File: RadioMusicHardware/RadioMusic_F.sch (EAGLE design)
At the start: 30 parts, among them X1 VERT_SD_CARD

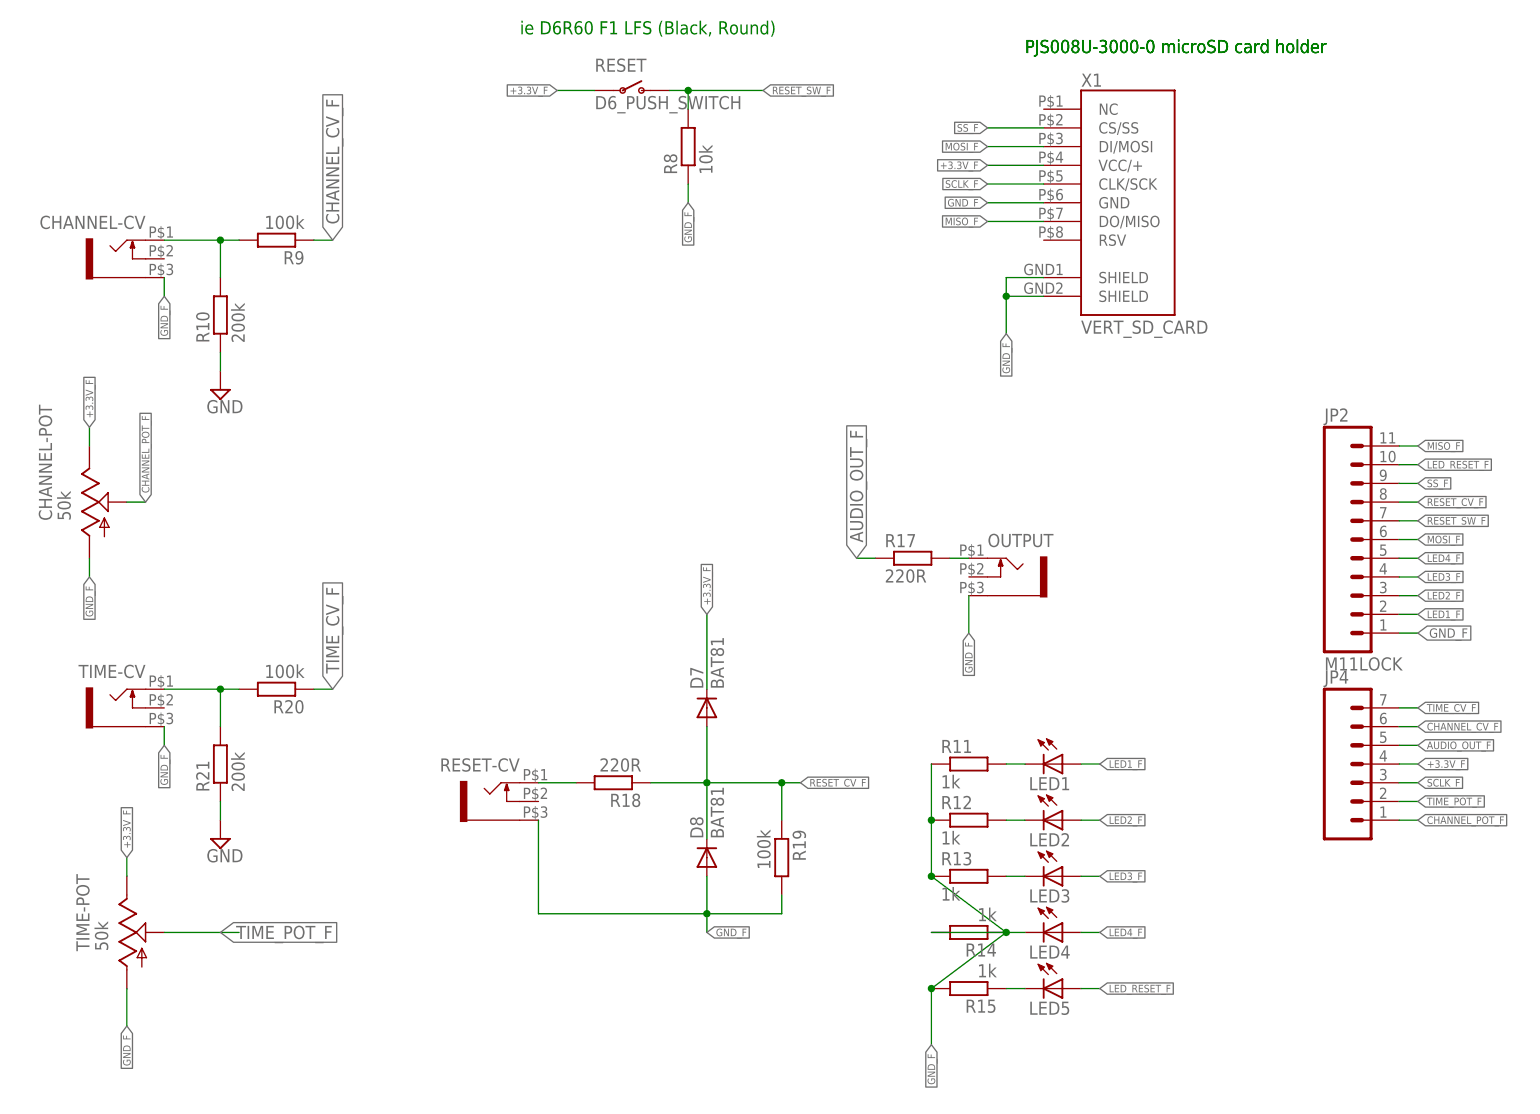
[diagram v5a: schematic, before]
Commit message: Fixed issues on Rev1 proto boards
Diodes changed to BAT42
LED resistors changed to 2k
Ground error on Front board fixed
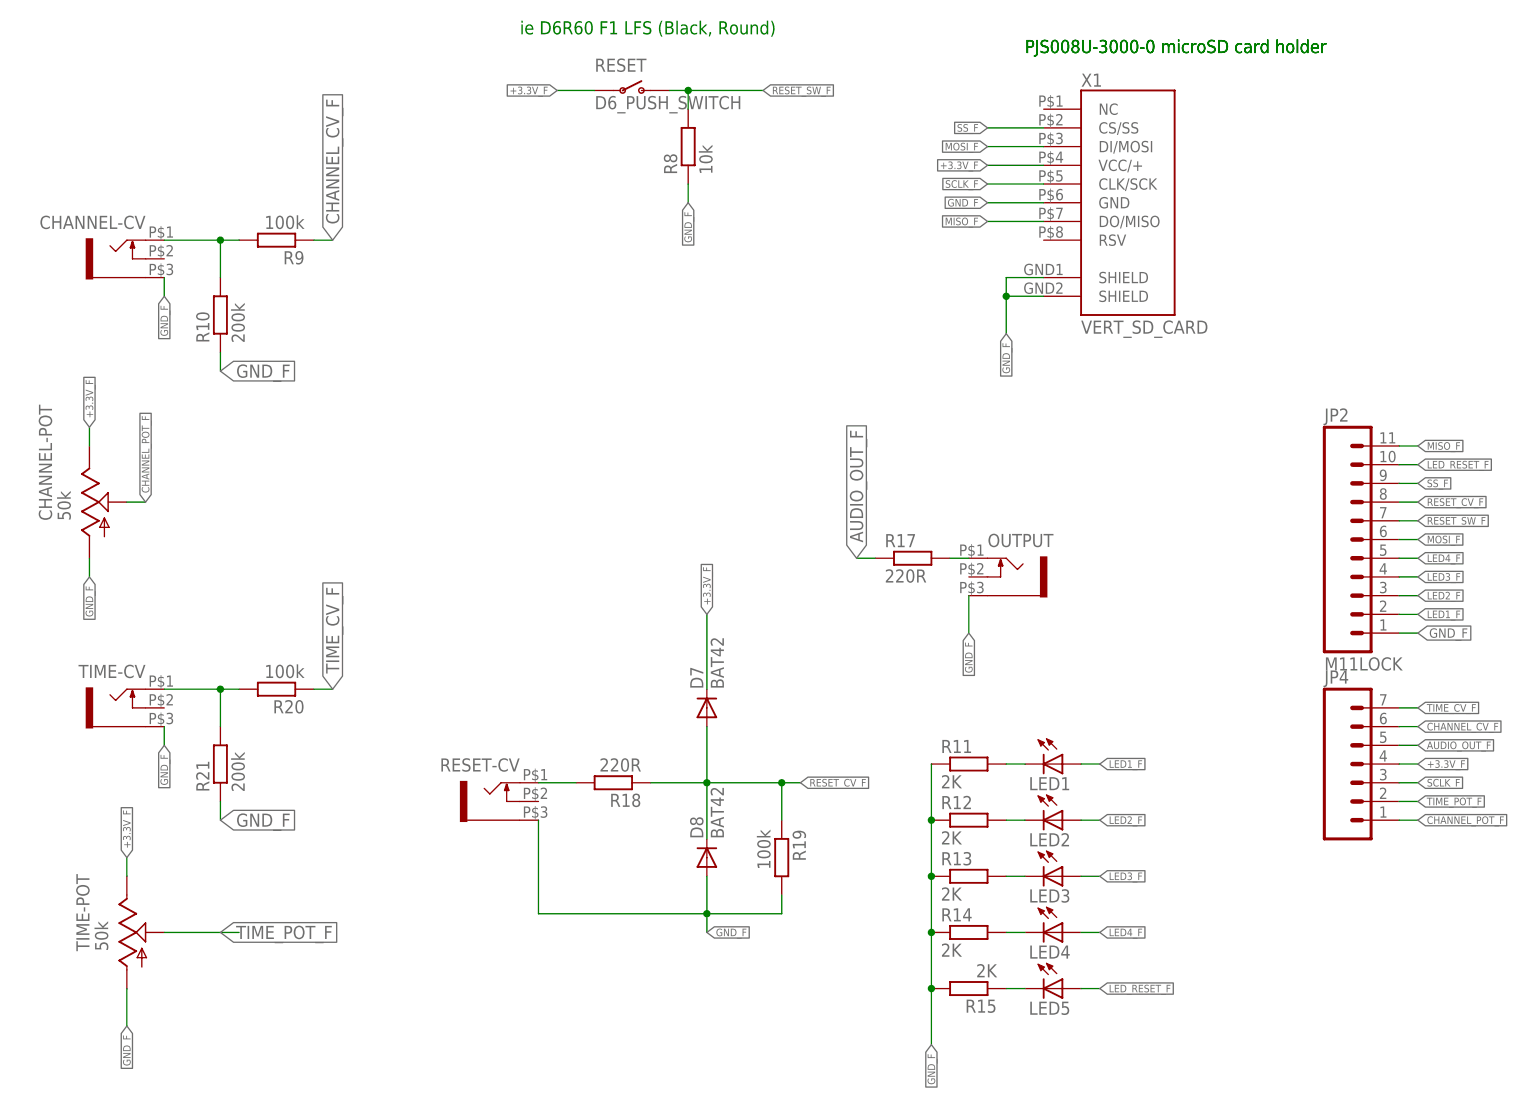
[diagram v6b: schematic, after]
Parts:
- D7, D8: value BAT81 -> BAT42
- R11, R12, R13, R14, R15: value 1k -> 2K
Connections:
- removed net GND: R10.1, R21.1
- net GND_F: now also R10.1, R21.1
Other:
- moved on the sheet: R14
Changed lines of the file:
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@@
 <part name="R9" library="TomW" deviceset="R-EU_" device="STANDARD_RESISTOR" value="100k"/>
 <part name="R10" library="TomW" deviceset="R-EU_" device="STANDARD_RESISTOR" value="200k"/>
-<part name="SUPPLY4" library="supply2" deviceset="GND" device=""/>
 <part name="R17" library="TomW" deviceset="R-EU_" device="STANDARD_RESISTOR" value="220R"/>
 <part name="TIME-POT" library="TomW" deviceset="ALPHA-9MM" device="A" technology="F2" value="50k"/>
@@
 <part name="R20" library="TomW" deviceset="R-EU_" device="STANDARD_RESISTOR" value="100k"/>
 <part name="R21" library="TomW" deviceset="R-EU_" device="STANDARD_RESISTOR" value="200k"/>
-<part name="SUPPLY5" library="supply2" deviceset="GND" device=""/>
-<part name="D7" library="diode" deviceset="BAT81" device=""/>
-<part name="D8" library="diode" deviceset="BAT81" device=""/>
+<part name="D7" library="diode" deviceset="BAT81" device="" value="BAT42"/>
+<part name="D8" library="diode" deviceset="BAT81" device="" value="BAT42"/>
 <part name="R19" library="TomW" deviceset="R-EU_" device="STANDARD_RESISTOR" value="100k"/>
 <part name="R18" library="TomW" deviceset="R-EU_" device="STANDARD_RESISTOR" value="220R"/>
@@
 <part name="LED3" library="TomW" deviceset="LED" device="3MM"/>
 <part name="LED4" library="TomW" deviceset="LED" device="3MM"/>
-<part name="R11" library="TomW" deviceset="R-EU_" device="STANDARD_RESISTOR" value="1k"/>
-<part name="R12" library="TomW" deviceset="R-EU_" device="STANDARD_RESISTOR" value="1k"/>
-<part name="R13" library="TomW" deviceset="R-EU_" device="STANDARD_RESISTOR" value="1k"/>
-<part name="R14" library="TomW" deviceset="R-EU_" device="STANDARD_RESISTOR" value="1k"/>
+<part name="R11" library="TomW" deviceset="R-EU_" device="STANDARD_RESISTOR" value="2K"/>
+<part name="R12" library="TomW" deviceset="R-EU_" device="STANDARD_RESISTOR" value="2K"/>
+<part name="R13" library="TomW" deviceset="R-EU_" device="STANDARD_RESISTOR" value="2K"/>
+<part name="R14" library="TomW" deviceset="R-EU_" device="STANDARD_RESISTOR" value="2K"/>
 <part name="X1" library="TomW" deviceset="VERT_SD_CARD" device=""/>
 <part name="LED5" library="TomW" deviceset="LED" device="3MM"/>
-<part name="R15" library="TomW" deviceset="R-EU_" device="STANDARD_RESISTOR" value="1k"/>
+<part name="R15" library="TomW" deviceset="R-EU_" device="STANDARD_RESISTOR" value="2K"/>
 <part name="JP2" library="SparkFun-Connectors" deviceset="M11" device="LOCK"/>
 <part name="JP4" library="SparkFun-Connectors" deviceset="M07" device="LOCK"/>
@@
 <instance part="R9" gate="G$1" x="50.8" y="116.84" rot="R180"/>
 <instance part="R10" gate="G$1" x="43.18" y="106.68" rot="R90"/>
-<instance part="SUPPLY4" gate="GND" x="43.18" y="96.52"/>
 <instance part="R17" gate="G$1" x="137.16" y="73.66"/>
 <instance part="TIME-POT" gate="G$1" x="30.48" y="22.86"/>
@@
 <instance part="R20" gate="G$1" x="50.8" y="55.88" rot="R180"/>
 <instance part="R21" gate="G$1" x="43.18" y="45.72" rot="R90"/>
-<instance part="SUPPLY5" gate="GND" x="43.18" y="35.56"/>
 <instance part="D7" gate="1" x="109.22" y="53.34" rot="R90"/>
 <instance part="D8" gate="1" x="109.22" y="33.02" rot="R90"/>
@@
 <instance part="R12" gate="G$1" x="144.78" y="38.1"/>
 <instance part="R13" gate="G$1" x="144.78" y="30.48"/>
-<instance part="R14" gate="G$1" x="144.78" y="22.86" rot="R180"/>
+<instance part="R14" gate="G$1" x="144.78" y="22.86"/>
 <instance part="X1" gate="G$1" x="162.56" y="121.92"/>
 <instance part="LED5" gate="G$1" x="157.48" y="15.24" rot="R270"/>
@@
 </busses>
 <nets>
-<net name="GND" class="2">
-<segment>
-<pinref part="R10" gate="G$1" pin="1"/>
-<wire x1="43.18" y1="101.6" x2="43.18" y2="99.06" width="0.1524" layer="91"/>
-<pinref part="SUPPLY4" gate="GND" pin="GND"/>
-</segment>
-<segment>
-<pinref part="R21" gate="G$1" pin="1"/>
-<wire x1="43.18" y1="40.64" x2="43.18" y2="38.1" width="0.1524" layer="91"/>
-<pinref part="SUPPLY5" gate="GND" pin="GND"/>
-</segment>
-</net>
 <net name="N$14" class="0">
 <segment>
@@
 <pinref part="LED4" gate="G$1" pin="C"/>
 <pinref part="R14" gate="G$1" pin="2"/>
-<wire x1="139.7" y1="22.86" x2="152.4" y2="22.86" width="0.1524" layer="91"/>
+<wire x1="149.86" y1="22.86" x2="152.4" y2="22.86" width="0.1524" layer="91"/>
 </segment>
 </net>
@@
 <junction x="139.7" y="38.1"/>
 <pinref part="R13" gate="G$1" pin="1"/>
-<wire x1="139.7" y1="30.48" x2="149.86" y2="22.86" width="0.1524" layer="91"/>
+<wire x1="139.7" y1="30.48" x2="139.7" y2="22.86" width="0.1524" layer="91"/>
 <junction x="139.7" y="30.48"/>
 <pinref part="R14" gate="G$1" pin="1"/>
-<wire x1="149.86" y1="22.86" x2="139.7" y2="15.24" width="0.1524" layer="91"/>
-<junction x="149.86" y="22.86"/>
+<wire x1="139.7" y1="22.86" x2="139.7" y2="15.24" width="0.1524" layer="91"/>
+<junction x="139.7" y="22.86"/>
 <pinref part="R15" gate="G$1" pin="2"/>
 <wire x1="139.7" y1="15.24" x2="139.7" y2="7.62" width="0.1524" layer="91"/>
@@
 <label x="205.74" y="63.5" size="1.27" layer="95" xref="yes"/>
 </segment>
-</net>
+<segment>
+<pinref part="R10" gate="G$1" pin="1"/>
+<wire x1="43.18" y1="99.06" x2="43.18" y2="101.6" width="0.1524" layer="91"/>
+<label x="43.18" y="99.06" size="1.778" layer="95" xref="yes"/>
+</segment>
+<segment>
+<pinref part="R21" gate="G$1" pin="1"/>
+<wire x1="43.18" y1="38.1" x2="43.18" y2="40.64" width="0.1524" layer="91"/>
+<label x="43.18" y="38.1" size="1.778" layer="95" xref="yes"/>
+</segment>
+</net>

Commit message: Change resistor values to reduce CV noise
Fixes #13
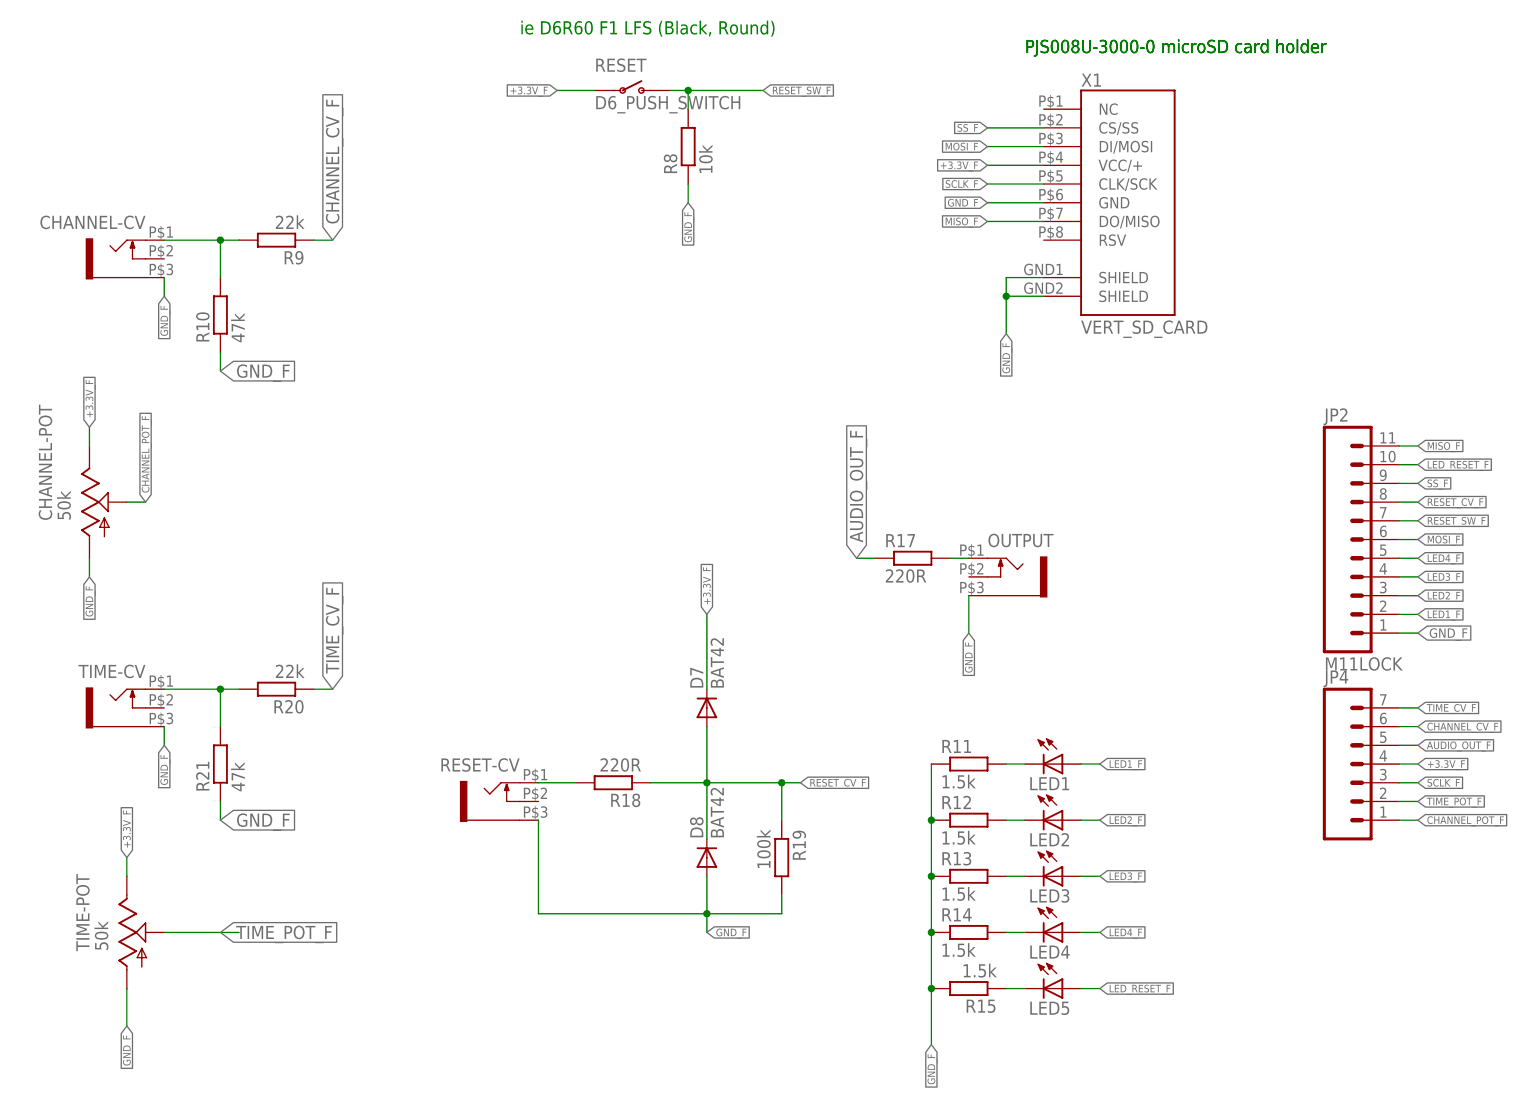
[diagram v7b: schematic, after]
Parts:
- R10, R21: value 200k -> 47k
- R11, R12, R13, R14, R15: value 2K -> 1.5k
- R20, R9: value 100k -> 22k
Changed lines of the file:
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@@
 <part name="RESET-CV" library="thonkiconn" deviceset="WQP-PJ301M-12_JACK" device="" value=""/>
 <part name="OUTPUT" library="thonkiconn" deviceset="WQP-PJ301M-12_JACK" device="" value=""/>
-<part name="R9" library="TomW" deviceset="R-EU_" device="STANDARD_RESISTOR" value="100k"/>
-<part name="R10" library="TomW" deviceset="R-EU_" device="STANDARD_RESISTOR" value="200k"/>
+<part name="R9" library="TomW" deviceset="R-EU_" device="STANDARD_RESISTOR" value="22k"/>
+<part name="R10" library="TomW" deviceset="R-EU_" device="STANDARD_RESISTOR" value="47k"/>
 <part name="R17" library="TomW" deviceset="R-EU_" device="STANDARD_RESISTOR" value="220R"/>
 <part name="TIME-POT" library="TomW" deviceset="ALPHA-9MM" device="A" technology="F2" value="50k"/>
 <part name="TIME-CV" library="thonkiconn" deviceset="WQP-PJ301M-12_JACK" device="" value=""/>
-<part name="R20" library="TomW" deviceset="R-EU_" device="STANDARD_RESISTOR" value="100k"/>
-<part name="R21" library="TomW" deviceset="R-EU_" device="STANDARD_RESISTOR" value="200k"/>
+<part name="R20" library="TomW" deviceset="R-EU_" device="STANDARD_RESISTOR" value="22k"/>
+<part name="R21" library="TomW" deviceset="R-EU_" device="STANDARD_RESISTOR" value="47k"/>
 <part name="D7" library="diode" deviceset="BAT81" device="" value="BAT42"/>
 <part name="D8" library="diode" deviceset="BAT81" device="" value="BAT42"/>
@@
 <part name="LED3" library="TomW" deviceset="LED" device="3MM"/>
 <part name="LED4" library="TomW" deviceset="LED" device="3MM"/>
-<part name="R11" library="TomW" deviceset="R-EU_" device="STANDARD_RESISTOR" value="2K"/>
-<part name="R12" library="TomW" deviceset="R-EU_" device="STANDARD_RESISTOR" value="2K"/>
-<part name="R13" library="TomW" deviceset="R-EU_" device="STANDARD_RESISTOR" value="2K"/>
-<part name="R14" library="TomW" deviceset="R-EU_" device="STANDARD_RESISTOR" value="2K"/>
+<part name="R11" library="TomW" deviceset="R-EU_" device="STANDARD_RESISTOR" value="1.5k"/>
+<part name="R12" library="TomW" deviceset="R-EU_" device="STANDARD_RESISTOR" value="1.5k"/>
+<part name="R13" library="TomW" deviceset="R-EU_" device="STANDARD_RESISTOR" value="1.5k"/>
+<part name="R14" library="TomW" deviceset="R-EU_" device="STANDARD_RESISTOR" value="1.5k"/>
 <part name="X1" library="TomW" deviceset="VERT_SD_CARD" device=""/>
 <part name="LED5" library="TomW" deviceset="LED" device="3MM"/>
-<part name="R15" library="TomW" deviceset="R-EU_" device="STANDARD_RESISTOR" value="2K"/>
+<part name="R15" library="TomW" deviceset="R-EU_" device="STANDARD_RESISTOR" value="1.5k"/>
 <part name="JP2" library="SparkFun-Connectors" deviceset="M11" device="LOCK"/>
 <part name="JP4" library="SparkFun-Connectors" deviceset="M07" device="LOCK"/>

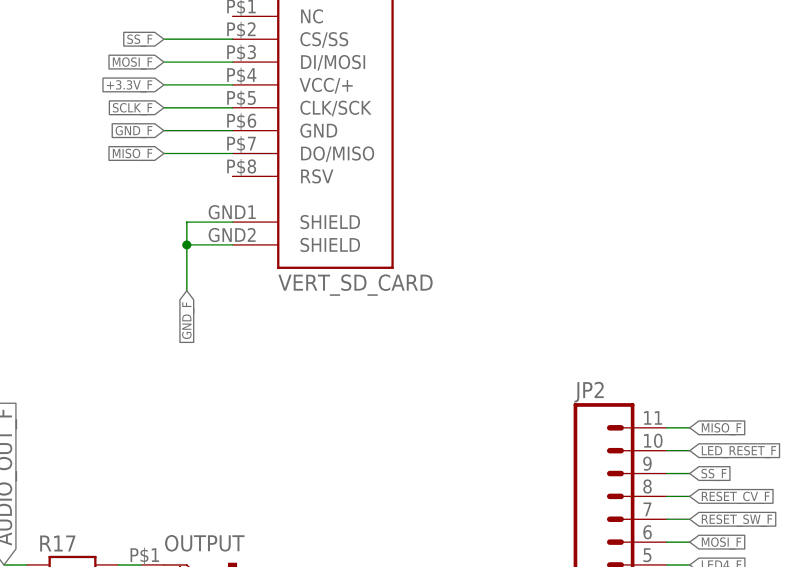
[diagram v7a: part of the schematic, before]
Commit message: Fix SD Card pin position
Pin holes were 0.5mm off Fixes #14
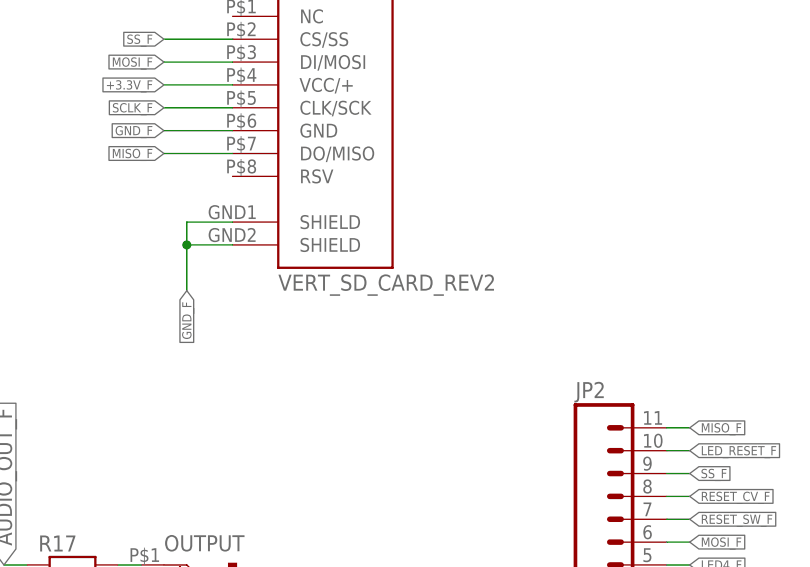
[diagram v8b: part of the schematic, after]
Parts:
- X1: value VERT_SD_CARD -> VERT_SD_CARD_REV2; device TomW:VERT_SD_CARD -> TomW:VERT_SD_CARD_REV2
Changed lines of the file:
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@@
 <part name="R13" library="TomW" deviceset="R-EU_" device="STANDARD_RESISTOR" value="1.5k"/>
 <part name="R14" library="TomW" deviceset="R-EU_" device="STANDARD_RESISTOR" value="1.5k"/>
-<part name="X1" library="TomW" deviceset="VERT_SD_CARD" device=""/>
+<part name="X1" library="TomW" deviceset="VERT_SD_CARD_REV2" device=""/>
 <part name="LED5" library="TomW" deviceset="LED" device="3MM"/>
 <part name="R15" library="TomW" deviceset="R-EU_" device="STANDARD_RESISTOR" value="1.5k"/>
